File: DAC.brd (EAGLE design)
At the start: 81.3 x 76.2 mm, 89 parts, among them IC1 LM2662, IC2 PCM1793, IC3 OPA2134PA, IC4 LMH6643, J1 USBSMD, J2 RCJ-21XXMILL, U1 LDO-TPS78233, U2 PCM2707, Y1 12MHz/20pF

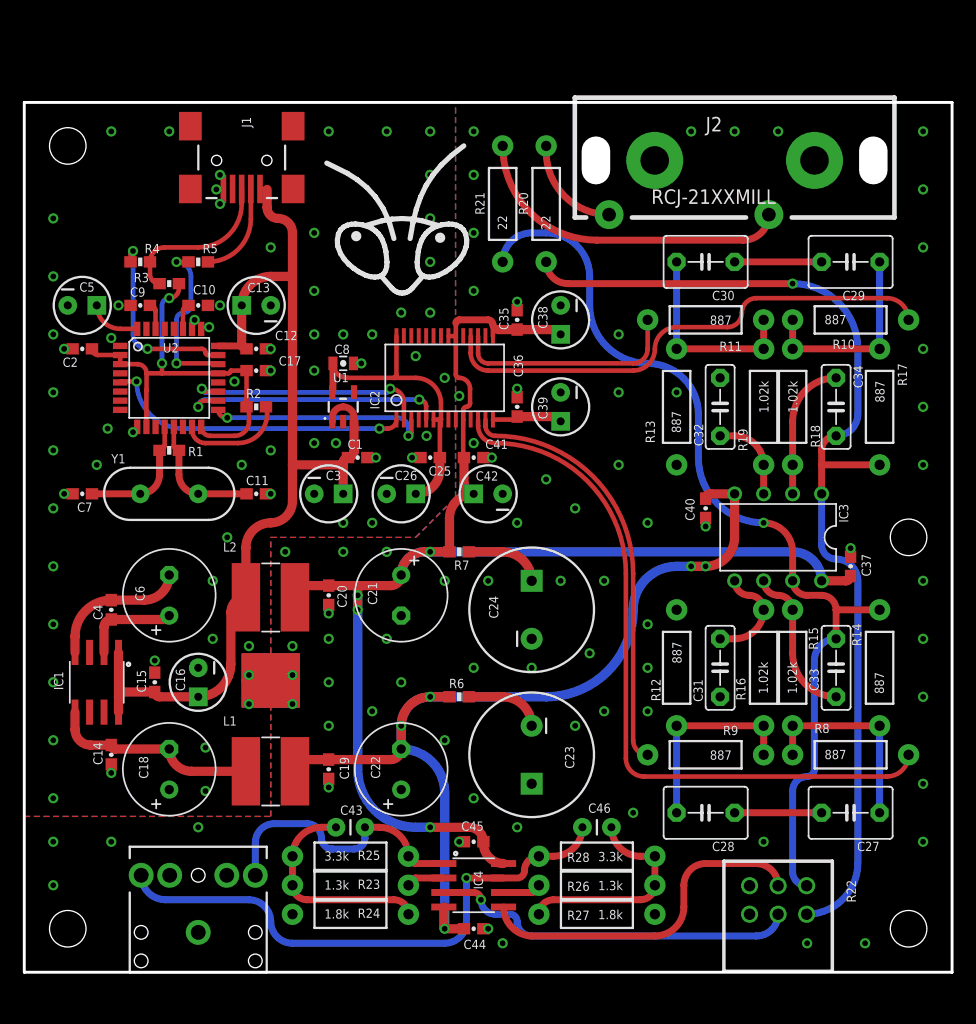
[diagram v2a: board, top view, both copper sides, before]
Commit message: More decoupling
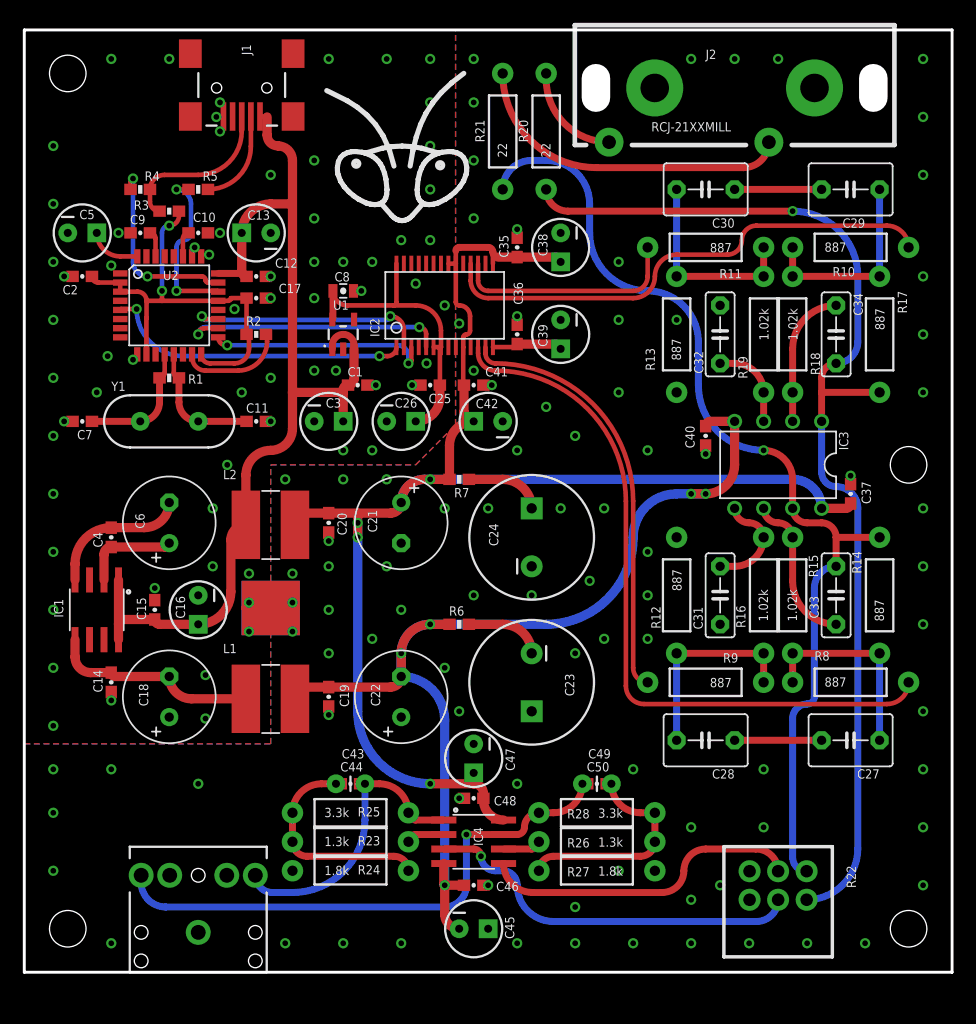
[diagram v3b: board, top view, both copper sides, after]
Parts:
- added C47: 10uF, SparkFun-Capacitors:CPOL-RADIAL-10UF-25V
- added C48: 0.1uF, SparkFun-Capacitors:0603-CAP
- added C49: 10pF, SparkFun-Capacitors:CAP-PTH-SMALL
- added C50: 10pF, SparkFun-Capacitors:0603-CAP
- C43: value 100pF -> 10pF
- C44: value 1.0uF -> 10pF
- C45: value 1.0uF -> 10uF; device SparkFun-Capacitors:0603-CAP -> SparkFun-Capacitors:CPOL-RADIAL-10UF-25V
- C46: value 100pF -> 0.1uF; device SparkFun-Capacitors:CAP-PTH-SMALL -> SparkFun-Capacitors:0603-CAP
- moved C44 16.7 mm to (28.6, 16.5), turned to 180 degrees
- moved C46 10.8 mm to (39.4, 7.62)
- moved C45 7.62 mm to (39.4, 3.81), turned to 0 degrees
- moved C1 6.35 mm to (29.2, 51.4)
- moved C11 6.35 mm to (20.3, 48.3)
- moved C12 6.35 mm to (20.3, 61.0)
- moved C15 6.35 mm to (11.4, 31.8)
- moved C16 6.35 mm to (15.2, 31.8)
- moved C17 6.35 mm to (20.3, 59.1)
- moved C2 6.35 mm to (5.08, 61.0)
- moved C24 6.35 mm to (44.5, 38.1)
- moved C25 6.35 mm to (35.6, 51.4)
- moved C26 6.35 mm to (33.0, 48.3)
- moved C29 6.35 mm to (72.4, 68.6)
- moved C3 6.35 mm to (26.7, 48.3)
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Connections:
- net +5V: now also C47.1, C48.1; no longer C45.1
- net -5V: now also C45.2, C46.1; no longer C44.1
- net AGND: now also C45.1, C46.2, C47.2, C48.2; no longer C44.2, C45.2
- net HP_L: now also C44.1
- net HP_R: now also C49.1, C50.1; no longer C46.1
- net N$14: now also C44.2
- net N$19: now also C49.2, C50.2; no longer C46.2
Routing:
- net -5V: track 84.3 -> 91.1 mm
- net OUT_L*: track 89.6 -> 94.6 mm
- net OUT_R*: track 79.2 -> 84.3 mm
- net +5V: track 123.8 -> 126.8 mm
- net N$15: track 29.7 -> 27.5 mm
- net N$12: track 31.7 -> 32.7 mm
- net HP_L: track 23.6 -> 24.7 mm
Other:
- board size 81.3 x 76.2 mm -> 81.3 x 82.5 mm

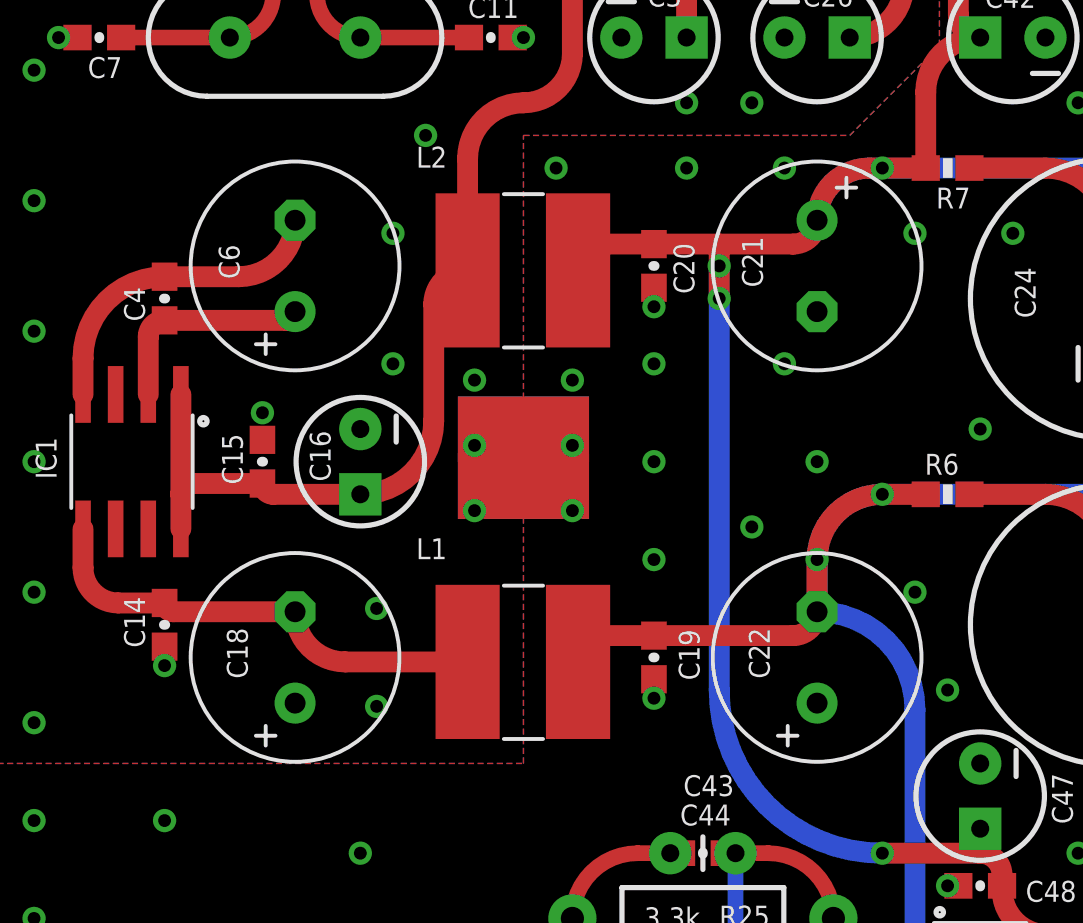
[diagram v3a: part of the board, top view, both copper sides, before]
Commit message: Caps footprint changed to more standard
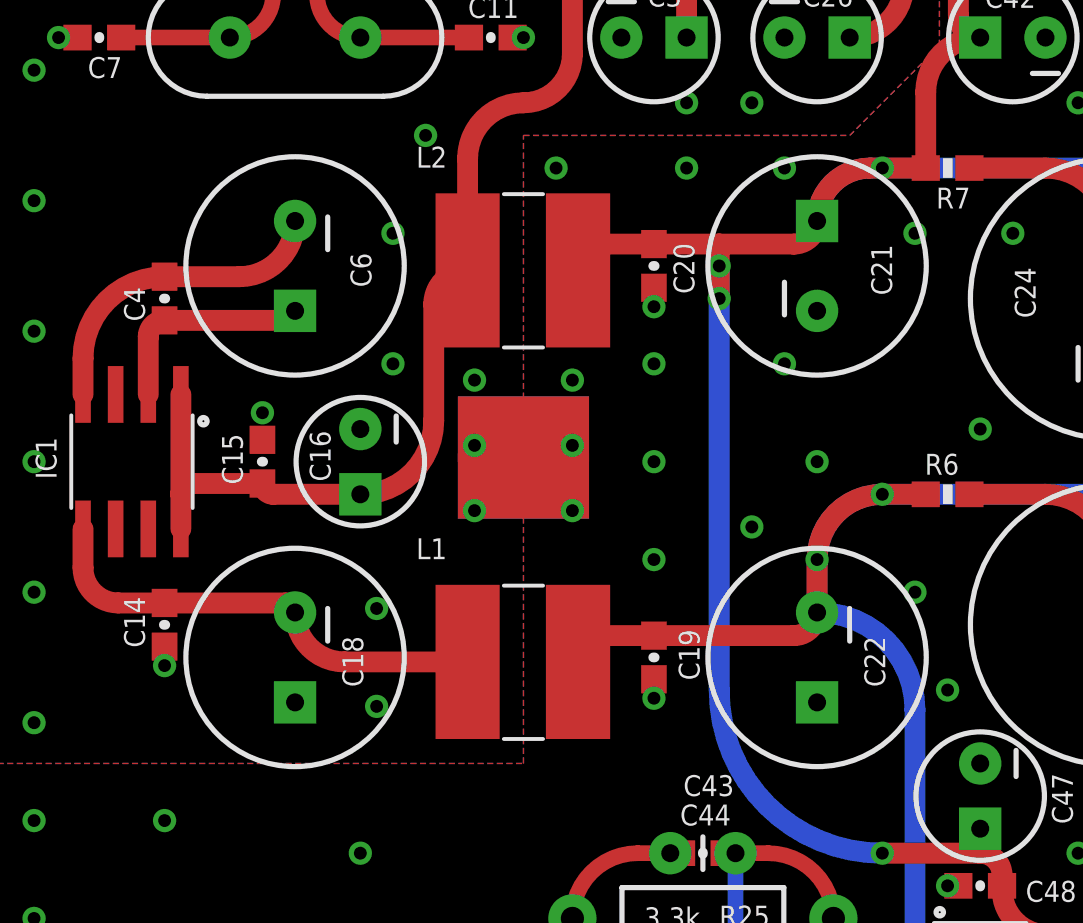
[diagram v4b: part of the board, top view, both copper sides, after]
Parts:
- C18, C21, C22, C6: device rcl:E3,5-8 -> my-cap:CPOL-RADIAL-8/3.5
- turned C18 to 270 degrees
- turned C21 to 90 degrees
- turned C22 to 270 degrees
- turned C6 to 270 degrees
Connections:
- net +5V: now also C21.1; no longer C21.+
- net -5V: now also C22.2; no longer C22.-
- net AGND: now also C21.2, C22.1; no longer C21.-, C22.+
- net GND: now also C18.1; no longer C18.+
- net N$11: now also C6.1; no longer C6.+
- net N$13: now also C6.2; no longer C6.-
- net N$9: now also C18.2; no longer C18.-

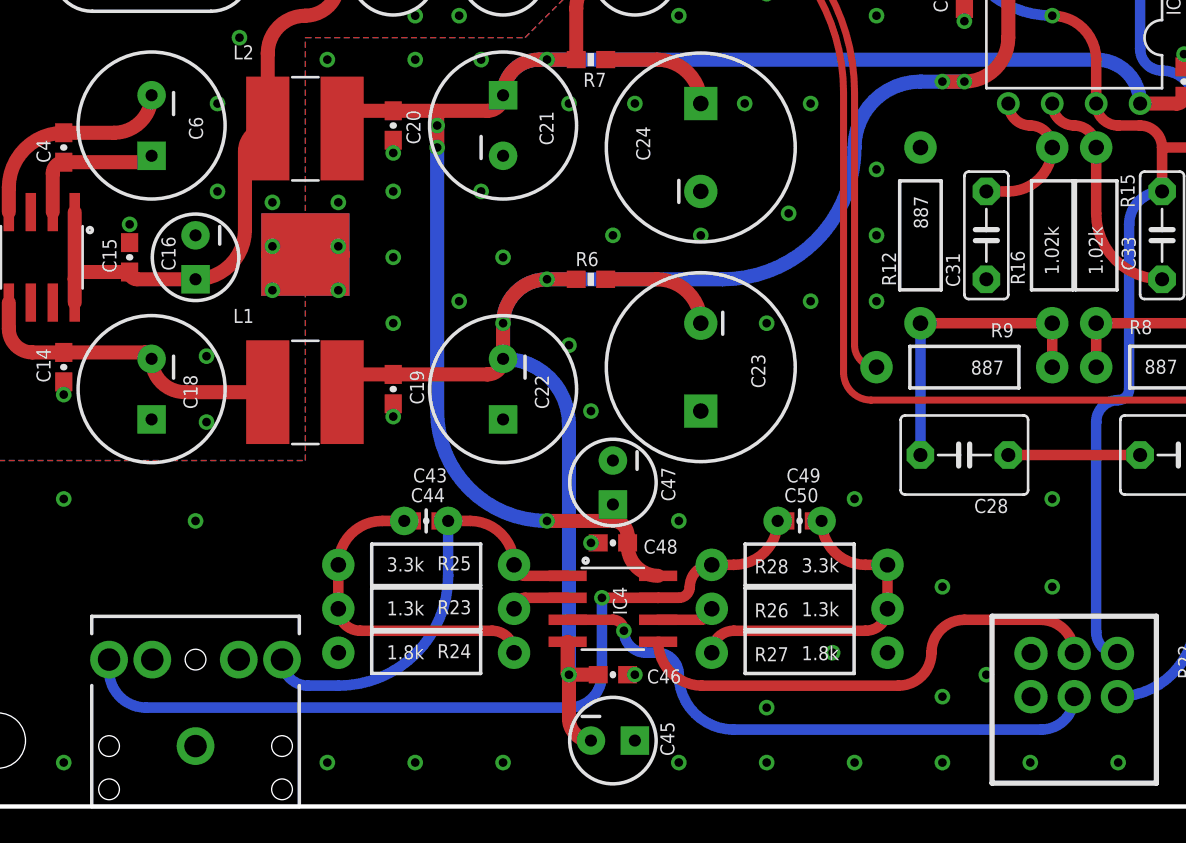
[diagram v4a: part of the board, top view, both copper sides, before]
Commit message: Power op amp is AC coupled now to avoid bias current to pass through the pot
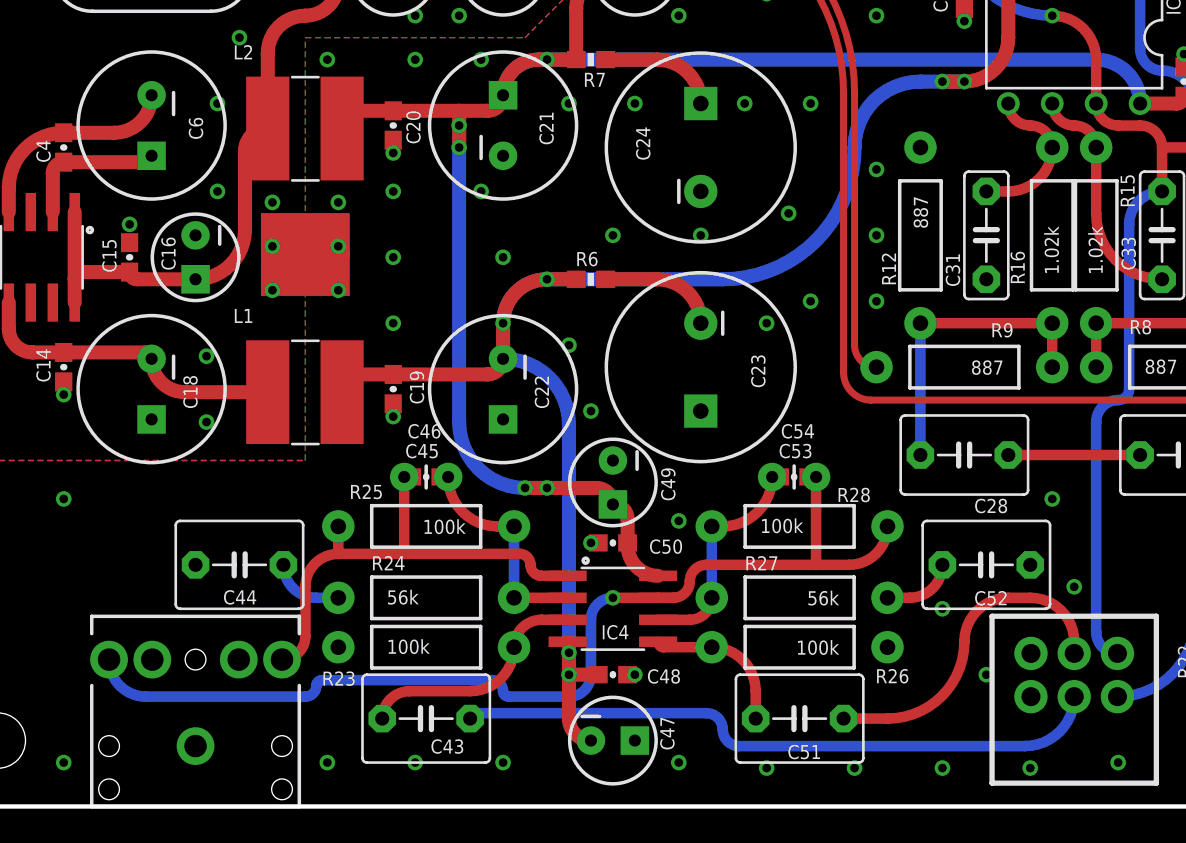
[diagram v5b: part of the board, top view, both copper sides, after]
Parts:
- added C51, C52: 2.2uF, capacitor-wima:C5B5
- added C53: 10pF, SparkFun-Capacitors:CAP-PTH-SMALL
- added C54: 10pF, SparkFun-Capacitors:0603-CAP
- C43: value 10pF -> 2.2uF; device SparkFun-Capacitors:CAP-PTH-SMALL -> capacitor-wima:C5B5
- C44: value 10pF -> 2.2uF; device SparkFun-Capacitors:0603-CAP -> capacitor-wima:C5B5
- C45: value 10uF -> 10pF; device SparkFun-Capacitors:CPOL-RADIAL-10UF-25V -> SparkFun-Capacitors:CAP-PTH-SMALL
- C46: value 0.1uF -> 10pF
- C49: value 10pF -> 10uF; device SparkFun-Capacitors:CAP-PTH-SMALL -> SparkFun-Capacitors:CPOL-RADIAL-10UF-25V
- C50: value 10pF -> 0.1uF
- R23, R26: value 1.3k -> 100k
- R24, R27: value 1.8k -> 56k
- R25, R28: value 3.3k -> 100k
- moved C45 19.4 mm to (27.3, 19.1)
- moved C46 15.7 mm to (28.6, 19.1)
- moved C47 14.9 mm to (39.4, 3.81), turned to 0 degrees
- moved C43 11.5 mm to (28.6, 5.08)
- moved C44 11.1 mm to (17.8, 14.0), turned to 0 degrees
- moved C50 10.9 mm to (39.4, 15.2), turned to 180 degrees
- moved C49 9.78 mm to (39.4, 18.7), turned to 270 degrees
- moved C48 7.62 mm to (39.4, 7.62), turned to 0 degrees
- moved R24 3.17 mm to (28.6, 12.1)
- moved R27 3.17 mm to (50.2, 12.1)
- moved R23 2.22 mm to (28.6, 9.21)
- moved R26 2.22 mm to (50.2, 9.21)
- moved R25 2.22 mm to (28.6, 16.2), turned to 180 degrees
- moved R28 2.22 mm to (50.2, 16.2), turned to 0 degrees
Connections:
- removed net N$6: IC4.6, R26.P$2
- new net N$23: C43.1, R22.R1.2
- new net N$24: C52.2, R27.P$1
- new net N$25: C44.2, R24.P$1
- net +5V: now also C49.1, C50.1; no longer C47.1, C48.1
- net -5V: now also C47.2, C48.1; no longer C45.2, C46.1
- net AGND: now also C44.1, C47.1, C49.2, C50.2, C52.1, R23.P$1, R26.P$1; no longer C45.1, C46.2, C47.2, R24.P$1, R27.P$1
- net HP_L: now also C45.1, C46.1; no longer C43.1, C44.1
- net HP_R: now also C53.1, C54.1; no longer C49.1, C50.1
- net N$12: now also C43.2, R23.P$2; no longer R22.R1.2
- net N$14: now also C51.1, R22.R2.2; no longer C43.2, C44.2, R23.P$1, R24.P$2, R25.P$1
- net N$15: now also C51.2, R26.P$2; no longer R22.R2.2
- net N$19: now also C53.2, C54.2, IC4.6; no longer C49.2, C50.2, R26.P$1
- net N$7: now also C45.2, C46.2, R24.P$2, R25.P$1; no longer R23.P$2
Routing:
- net N$23: track 0.00 -> 37.0 mm
- net N$12: track 32.7 -> 13.1 mm, vias 1 -> 0
- net N$15: track 27.5 -> 8.41 mm
- net HP_R: track 47.7 -> 58.1 mm
- net N$7: track 3.36 -> 12.6 mm
- net N$19: track 19.0 -> 12.8 mm
- net N$24: track 0.00 -> 3.96 mm
- net N$25: track 0.00 -> 3.96 mm
- net N$6: track 3.36 -> 0.00 mm
- net HP_L: track 24.7 -> 27.7 mm
- net N$14: track 19.0 -> 18.0 mm
- net +5V: vias 4 -> 5
- net -5V: vias 5 -> 6
